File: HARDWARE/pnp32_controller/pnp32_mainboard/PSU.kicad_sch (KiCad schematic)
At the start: 51 parts, among them J1 COMBO_POWER_JACK, U1 FDS4435BZ, U2 FDS4435BZ, U3 TPS54560BDDA, U4 AP1117-33

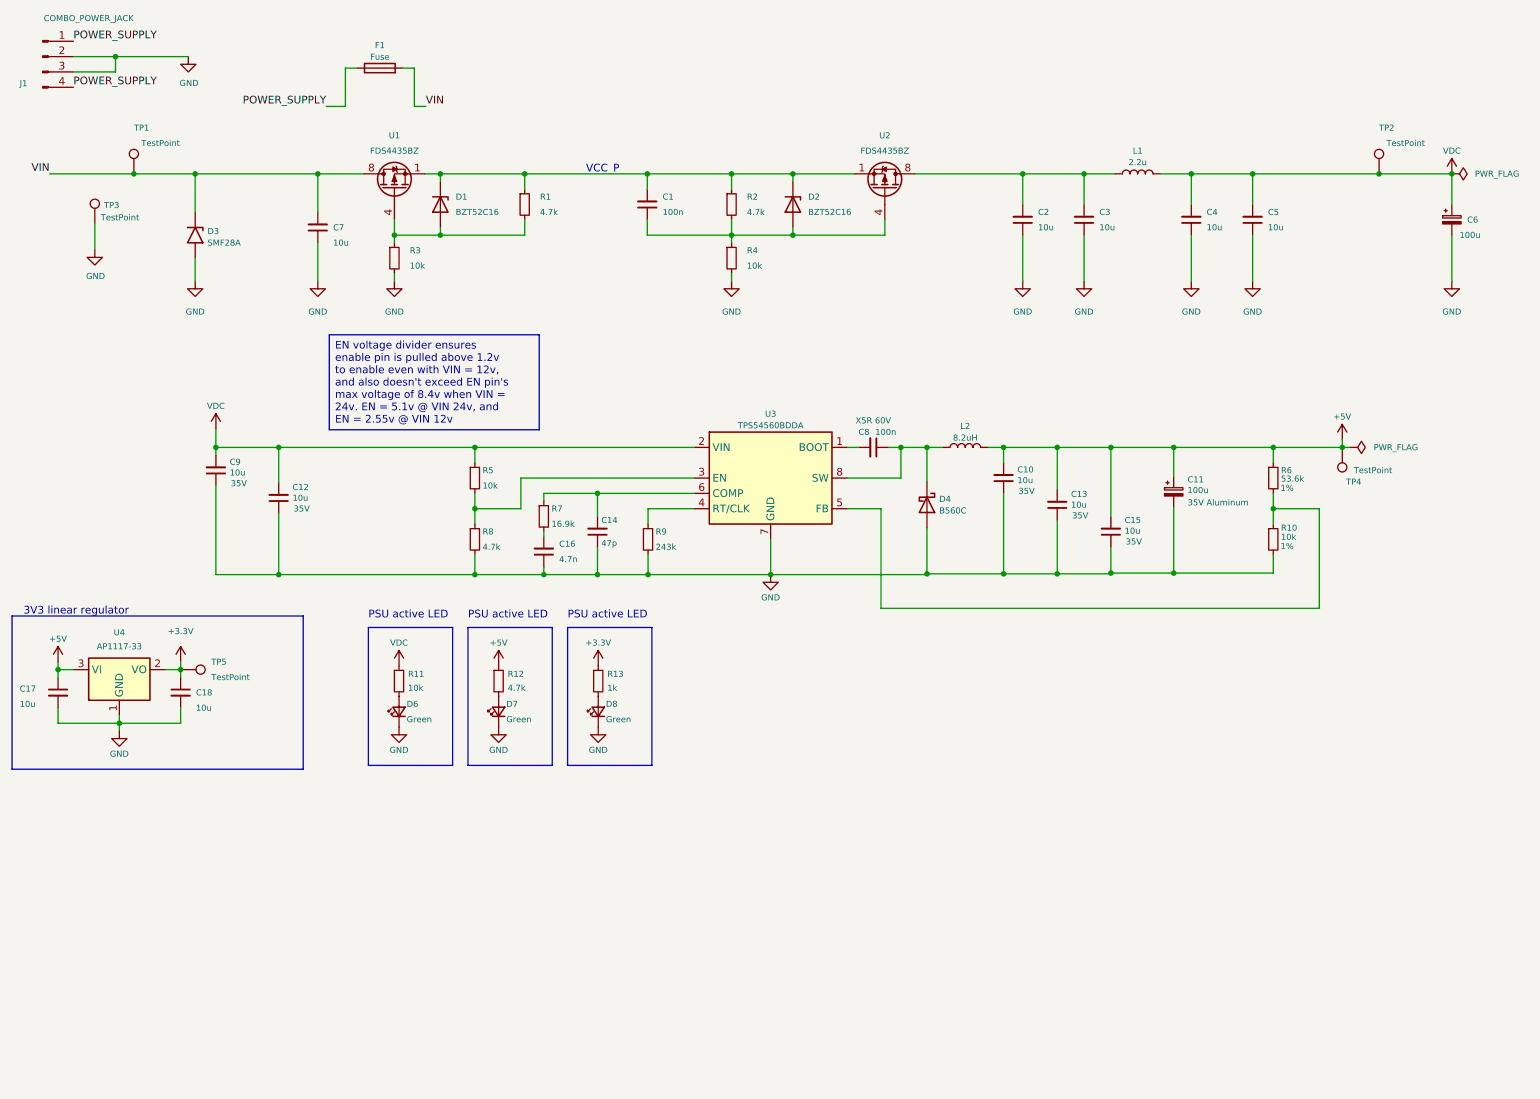
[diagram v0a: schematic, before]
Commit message: update_PSU
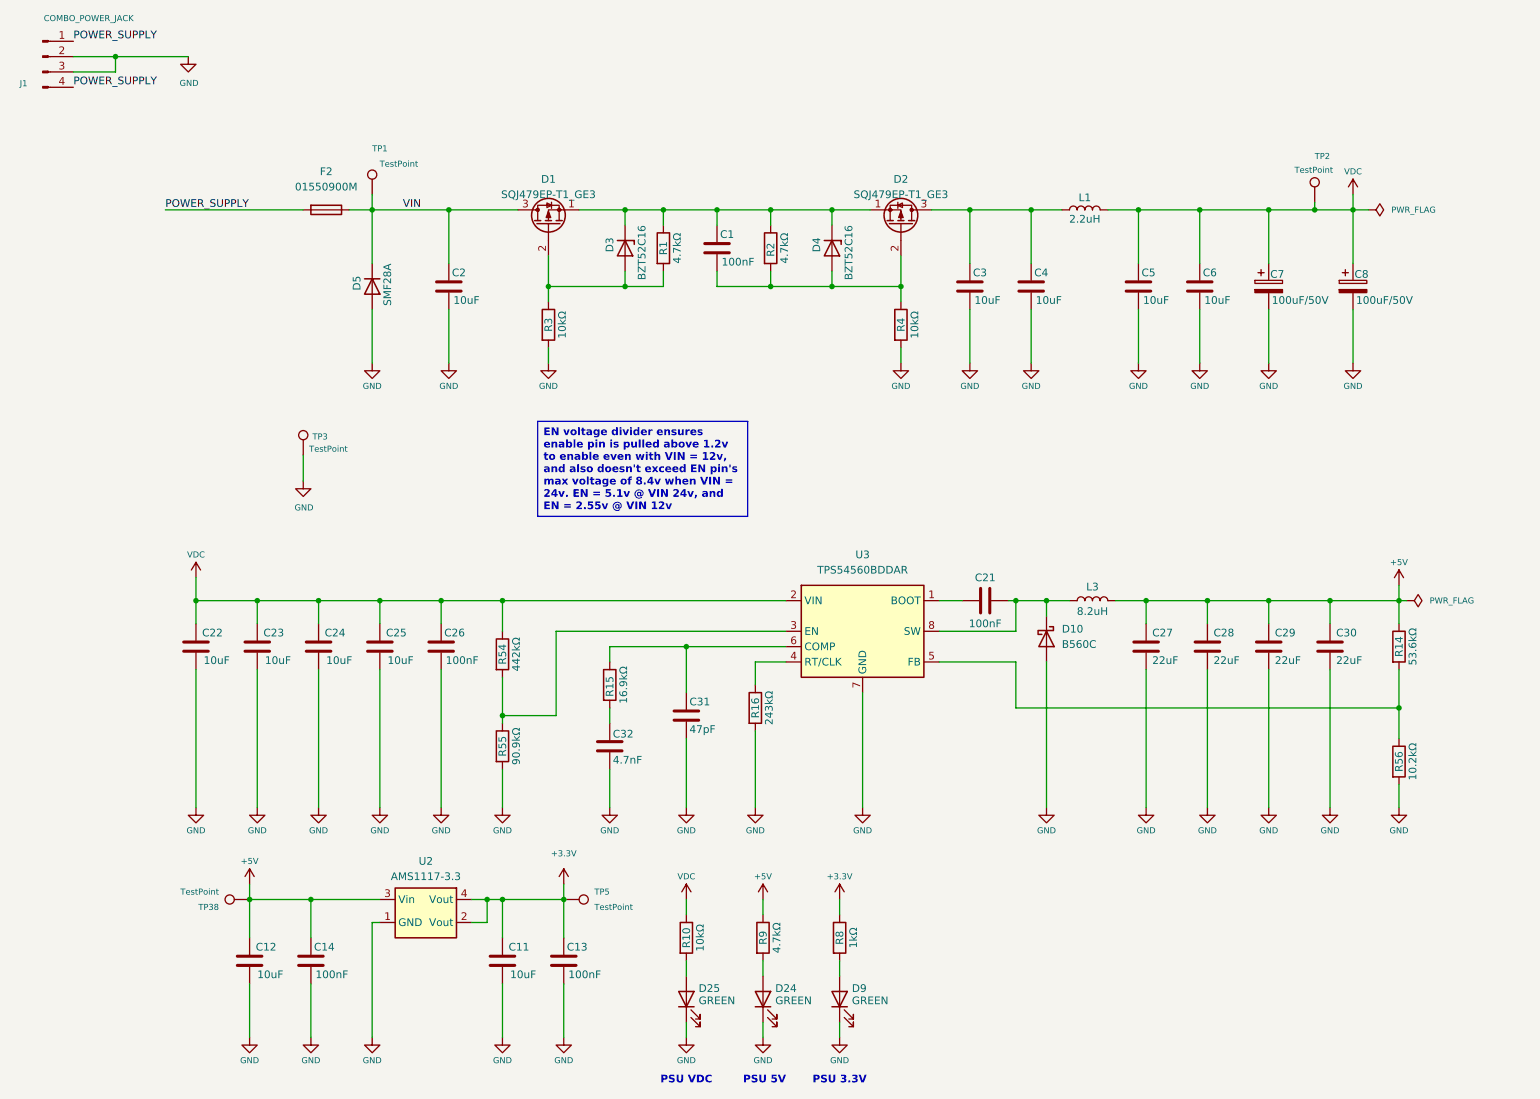
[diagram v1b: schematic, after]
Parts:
- removed C1, C8: 100n, Capacitor_SMD:C_0805_2012Metric, symbol Device:C_Small
- removed C10, C12, C13, C15, C17, C18, C2, C3, C4, C5, C7, C9: 10u, Capacitor_SMD:C_0805_2012Metric, symbol Device:C_Small
- removed C11, C6: 100u, Capacitor_SMD:CP_Elec_6.3x7.7, symbol Device:C_Polarized_Small
- removed C14: 47p, Capacitor_SMD:C_0805_2012Metric, symbol Device:C_Small
- removed C16: 4.7n, Capacitor_SMD:C_0805_2012Metric, symbol Device:C_Small
- removed D1, D2: BZT52C16, Diode_SMD:D_SOD-123, symbol Diode:BZT52Bxx
- removed D3: SMF28A, Diode_SMD:D_SMF, symbol Diode:SMF28A
- removed D4: B560C, Diode_SMD:D_SMC, symbol Device:D_Schottky
- removed D6, D7, D8: Green, LED_SMD:LED_0805_2012Metric, symbol Device:LED_Small
- removed F1: Fuse, Fuse:Fuseholder_Littelfuse_Nano2_154x, symbol Device:Fuse
- removed L1: 2.2u, Inductor_SMD:L_Sunlord_MWSA0402S, symbol Device:L
- removed L2: 8.2uH, Inductor_SMD:L_Sunlord_MWSA0603S, symbol Device:L
- removed R1, R12, R2, R8: 4.7k, Resistor_SMD:R_0805_2012Metric, symbol Device:R_Small
- removed R10, R11, R3, R4, R5: 10k, Resistor_SMD:R_0805_2012Metric, symbol Device:R_Small
- removed R13: 1k, Resistor_SMD:R_0805_2012Metric, symbol Device:R_Small
- removed R6: 53.6k, Resistor_SMD:R_0805_2012Metric, symbol Device:R_Small
- removed R7: 16.9k, Resistor_SMD:R_0805_2012Metric, symbol Device:R_Small
- removed R9: 243k, Resistor_SMD:R_0805_2012Metric, symbol Device:R_Small
- removed TP4: TestPoint, TestPoint:TestPoint_Pad_D2.0mm, symbol Connector:TestPoint
- removed U1, U2: FDS4435BZ, Package_SO:SO-8_3.9x4.9mm_P1.27mm, symbol index:FDS4435BZ
- removed U3: TPS54560BDDA, Package_SO:Texas_R-PDSO-G8_EP2.95x4.9mm_Mask2.4x3.1mm_ThermalVias, symbol Regulator_Switching:TPS54560BDDA
- removed U4: AP1117-33, Package_TO_SOT_SMD:SOT-223-3_TabPin2, symbol Regulator_Linear:AP1117-33
- added C1, C13, C14, C21, C26: 100nF, fab_C:C_0603, symbol fab_C:C_100nF_0603_50V
- added C11, C12, C2, C22, C23, C24, C25, C3, C4, C5, C6: 10uF, fab_C:C_1210, symbol fab_C:C_10uF_1210_50V
- added C27, C28, C29, C30: 22uF, fab_C:C_1210, symbol fab_C:C_22uF_1210
- added C31: 47pF, fab_C:C_0603, symbol fab_C:C_47pF_0603
- added C32: 4.7nF, fab_C:C_0603, symbol fab_C:C_4.7nF_0603
- added C7, C8: 100uF/50V, fab_C_Pol:CP_Elec_8x10.5, symbol fab_C_Pol:C_Pol_100uF_SMD,D8xL10.5mm
- added D1, D2: SQJ479EP-T1_GE3, fab_T:PowerPAK_SO-8L_Single, symbol fab_T:SQJ479EP-T1_GE3
- added D10: B560C, fab_D:SMC, symbol fab_D:B560C
- added D24, D25, D9: GREEN, fab_D:LED_0603_1608Metric, symbol fab_D:KT-0603R
- added D3, D4: BZT52C16, fab_D:SOD-123, symbol fab_D:BZT52C16
- added D5: SMF28A, fab_D:SOD-123FL, symbol fab_D:SMF28A
- added F2: 01550900M, fab_F:Fuseholder_Littelfuse_Nano2_154x, symbol fab_F:F_01550900M
- added L1: 2.2uH, fab_L:L_Sunlord_MWSA0402S, symbol fab_L:L_2.2uH_SMD,4.4x4.2mm
- added L3: 8.2uH, fab_L:L_Changjiang_FXL0630, symbol fab_L:L_8.2uH_SMD,6.6x7mm
- added R1, R2, R9: 4.7kΩ, fab_R:R_0603, symbol fab_R:R_4.7kΩ_0603
- added R10, R3, R4: 10kΩ, fab_R:R_0603, symbol fab_R:R_10kΩ_0603
- added R14: 53.6kΩ, fab_R:R_0603, symbol fab_R:R_53.6kΩ_0603
- added R15: 16.9kΩ, fab_R:R_0603, symbol fab_R:R_16.9kΩ_0603
- added R16: 243kΩ, fab_R:R_0603, symbol fab_R:R_243kΩ_0603
- added R54: 442kΩ, fab_R:R_0603, symbol fab_R:R_442kΩ_0603
- added R55: 90.9kΩ, fab_R:R_0603, symbol fab_R:R_90.9kΩ_0603
- added R56: 10.2kΩ, fab_R:R_0603, symbol fab_R:R_10.2kΩ_0603
- added R8: 1kΩ, fab_R:R_0603, symbol fab_R:R_1kΩ_0603
- added TP38: TestPoint, TestPoint:TestPoint_Pad_D2.0mm, symbol Connector:TestPoint
- added U2: AMS1117-3.3, fab_U:SOT-223, symbol fab_U:AMS1117-3.3
- added U3: TPS54560BDDAR, fab_U:Texas_HSOP-8-1EP_3.9x4.9mm_P1.27mm_ThermalVias, symbol fab_U:TPS54560BDDAR
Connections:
- net +3.3V: now also C11.1, C13.1, R8.1, U2.2 (Vout), U2.4 (Vout)
- net +5V: now also C12.1, C14.1, C27.1, C28.1, C29.1, C30.1, L3.2, R14.1, R9.1, TP38.1, U2.3 (Vin)
- net GND: now also C11.2, C12.2, C13.2, C14.2, C2.2, C22.2, C23.2, C24.2, C25.2, C26.2, C27.2, C28.2, C29.2, C3.2, C30.2, C31.2, C32.2, C4.2, C5.2, C6.2, C7.2, C8.2, D10.2 (A2), D24.1 (K), D25.1 (K), D5.2 (A2), D9.1 (K), R16.2, R3.2, R4.2, R55.2, R56.2, U2.1 (GND), U3.7 (GND), U3.9 (GND)
- net POWER_SUPPLY: now also F2.1
- net VDC: now also C22.1, C23.1, C24.1, C25.1, C26.1, C5.1, C6.1, C7.1, C8.1, L1.2, R10.1, R54.1, U3.2 (VIN)
- net VIN: now also C2.1, D1.3 (D), D5.1 (A1), F2.2
- new net: C1.1, D1.1 (S), D2.1 (S), D3.1 (K), D4.1 (K), R1.1, R2.1
- new net: C1.2, D2.2 (G), D4.2 (A), R2.2, R4.1
- new net: C31.1, R15.1, U3.6 (COMP)
- new net: D25.2 (A), R10.2
- new net: R14.2, R56.1, U3.5 (FB)
- new net: D9.2 (A), R8.2
- new net: R54.2, R55.1, U3.3 (EN)
- new net: C21.1, U3.1 (BOOT)
- new net: C21.2, D10.1 (A1), L3.1, U3.8 (SW)
- new net: C3.1, C4.1, D2.3 (D), L1.1
- new net: R16.1, U3.4 (RT/CLK)
- new net: C32.1, R15.2
- new net: D24.2 (A), R9.2
- new net: D1.2 (G), D3.2 (A), R1.2, R3.1
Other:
- note added: "PSU 3.3V"
- note added: "PSU 5V"
- note added: "PSU VDC"
- note removed: "3V3 linear regulator"
- note removed: "PSU active LED"
- note removed: "VCC_P"
